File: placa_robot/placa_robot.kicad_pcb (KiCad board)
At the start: 2 copper layers, 75 x 80 mm, 26 parts, among them IC1 MSP430FR2355TPT, J1 Conn_01x03, J2 Conn_01x01, J3 Conn_02x04_Odd_Even, J4 conn_DFrobot, SW1 SW_Push, U1 LM324, Y1 Crystal

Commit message: Desacoplos y limitador
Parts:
- added C6: 100n, Capacitor_SMD:C_0805_2012Metric_Pad1.18x1.45mm_HandSolder, F.Cu at (86.0, 70.5)
- added TP1: TestPoint, Connector_PinHeader_2.54mm:PinHeader_1x01_P2.54mm_Vertical, F.Cu at (78.5, 53.7)
- added TP10: TestPoint, Connector_PinHeader_2.54mm:PinHeader_1x01_P2.54mm_Vertical, F.Cu at (83.2, 53.7)
- added TP11: TestPoint, Connector_PinHeader_2.54mm:PinHeader_1x01_P2.54mm_Vertical, F.Cu at (83.2, 58.4)
- added TP12: TestPoint, Connector_PinHeader_2.54mm:PinHeader_1x01_P2.54mm_Vertical, F.Cu at (83.2, 63.0)
- added TP13: TestPoint, Connector_PinHeader_2.54mm:PinHeader_1x01_P2.54mm_Vertical, F.Cu at (87.8, 53.7)
- added TP14: TestPoint, Connector_PinHeader_2.54mm:PinHeader_1x01_P2.54mm_Vertical, F.Cu at (87.8, 58.4)
- added TP15: TestPoint, Connector_PinHeader_2.54mm:PinHeader_1x01_P2.54mm_Vertical, F.Cu at (87.8, 63.0)
- added TP16: TestPoint, Connector_PinHeader_2.54mm:PinHeader_1x01_P2.54mm_Vertical, F.Cu at (92.5, 53.7)
- added TP17: TestPoint, Connector_PinHeader_2.54mm:PinHeader_1x01_P2.54mm_Vertical, F.Cu at (92.5, 58.4)
- added TP18: TestPoint, Connector_PinHeader_2.54mm:PinHeader_1x01_P2.54mm_Vertical, F.Cu at (92.5, 63.0)
- added TP2: TestPoint, Connector_PinHeader_2.54mm:PinHeader_1x01_P2.54mm_Vertical, F.Cu at (78.5, 58.4)
- added TP6: TestPoint, Connector_PinHeader_2.54mm:PinHeader_1x01_P2.54mm_Vertical, F.Cu at (78.5, 63.0)
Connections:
- net Net-(IC1-P2.6/MCLK/XOUT) renamed /XOUT
- net Net-(IC1-P2.7/TB0CLK/XIN) renamed /XIN
- IC1 pad 6: unconnected-(IC1-DVCC-Pad6) -> +3.3V
- IC1 pad 7: unconnected-(IC1-DVSS-Pad7) -> GND
- JP1 pad 1: +3.3V -> /Pantalla_LCD
- LCD1 pad 6: +3.3V -> /Pantalla_LCD
- LCD1 pad 7: GND -> Net-(LCD1-K)
- RV1 pad 1: unconnected-(RV1-Pad1) -> /Photo2
- RV1 pad 2: /Photo2 -> GND
- RV2 pad 1: unconnected-(RV2-Pad1) -> /Photo1
- RV2 pad 2: /Photo1 -> GND
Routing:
- net /XOUT: track 0.00 -> 3.86 mm
- net /XIN: track 0.00 -> 3.28 mm
- net GND: track 1.50 -> 4.03 mm, vias 1 -> 2

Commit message: Errores layout
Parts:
- removed TP1, TP10, TP11, TP12, TP13, TP14, TP15, TP16, TP17, TP18, TP2, TP6: TestPoint, Connector_PinHeader_2.54mm:PinHeader_1x01_P2.54mm_Vertical
- added C7: 100n, Capacitor_SMD:C_0805_2012Metric_Pad1.18x1.45mm_HandSolder, F.Cu at (141.5, 111.2)
- added R1: 1k, Resistor_SMD:R_0805_2012Metric_Pad1.20x1.40mm_HandSolder, F.Cu at (165.2, 67.2)
- R10, R9: footprint Connector_PinHeader_2.54mm:PinHeader_1x02_P2.54mm_Horizontal -> Connector_PinHeader_2.54mm:PinHeader_1x02_P2.54mm_Vertical
- moved C6 67.4 mm to (153.2, 73.8), turned to 180 degrees
- moved C4 15.1 mm to (149.0, 65.6), turned to 180 degrees
- moved C2 13.4 mm to (149.2, 71.2), turned to 180 degrees
- moved R10 2.75 mm to (179.0, 117.2)
- moved S2 2.28 mm to (141.6, 100.6)
- moved R9 2.24 mm to (114.5, 118.0)
- moved JP1 2.00 mm to (179.0, 66.2)
- moved Y1 0.99 mm to (148.0, 69.3)
- moved J2 0.75 mm to (168.2, 118.0)
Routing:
- net GND: track 4.03 -> 21.9 mm, vias 2 -> 10
- net +3.3V: track 11.0 -> 27.1 mm
- net /Pantalla_LCD: track 0.00 -> 7.64 mm
- net /Photo1: track 77.9 -> 82.3 mm
- net Net-(LCD1-K): track 0.00 -> 3.28 mm
- net /XOUT: track 3.86 -> 6.95 mm
- net /XIN: track 3.28 -> 6.04 mm
- net Net-(S2-2'): track 16.4 -> 19.0 mm
- net /JOY_BOTTON: track 63.5 -> 65.9 mm
- net /P2: track 13.4 -> 11.7 mm
- net Net-(U1C--): track 36.0 -> 37.6 mm
- net /Photo2: track 61.8 -> 63.2 mm
- net /P1: track 15.7 -> 14.3 mm
- net /P0: track 17.3 -> 16.0 mm
- net /LEFT: track 9.80 -> 10.4 mm
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
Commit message: Placa acabada
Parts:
- removed C3: 100n, Capacitor_SMD:C_0805_2012Metric_Pad1.18x1.45mm_HandSolder
- moved R13 3.60 mm to (175.4, 58.5)
- moved R14 3.60 mm to (175.4, 54.5)
- moved C6 0.21 mm to (153.5, 73.8)
- moved C4 0.14 mm to (149.1, 65.6)
- moved Y1 0.07 mm to (148.1, 69.3)
- moved C2 0.06 mm to (149.1, 71.2)
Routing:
- net +3.3V: track 27.1 -> 32.2 mm, vias 0 -> 6
- net /MCU_RST: track 81.0 -> 85.7 mm
- net GND: track 21.9 -> 26.3 mm
- net /SDA: track 79.9 -> 76.3 mm
- net /SCL: track 80.3 -> 77.4 mm
- net /WIFI_RXD: track 60.2 -> 61.1 mm

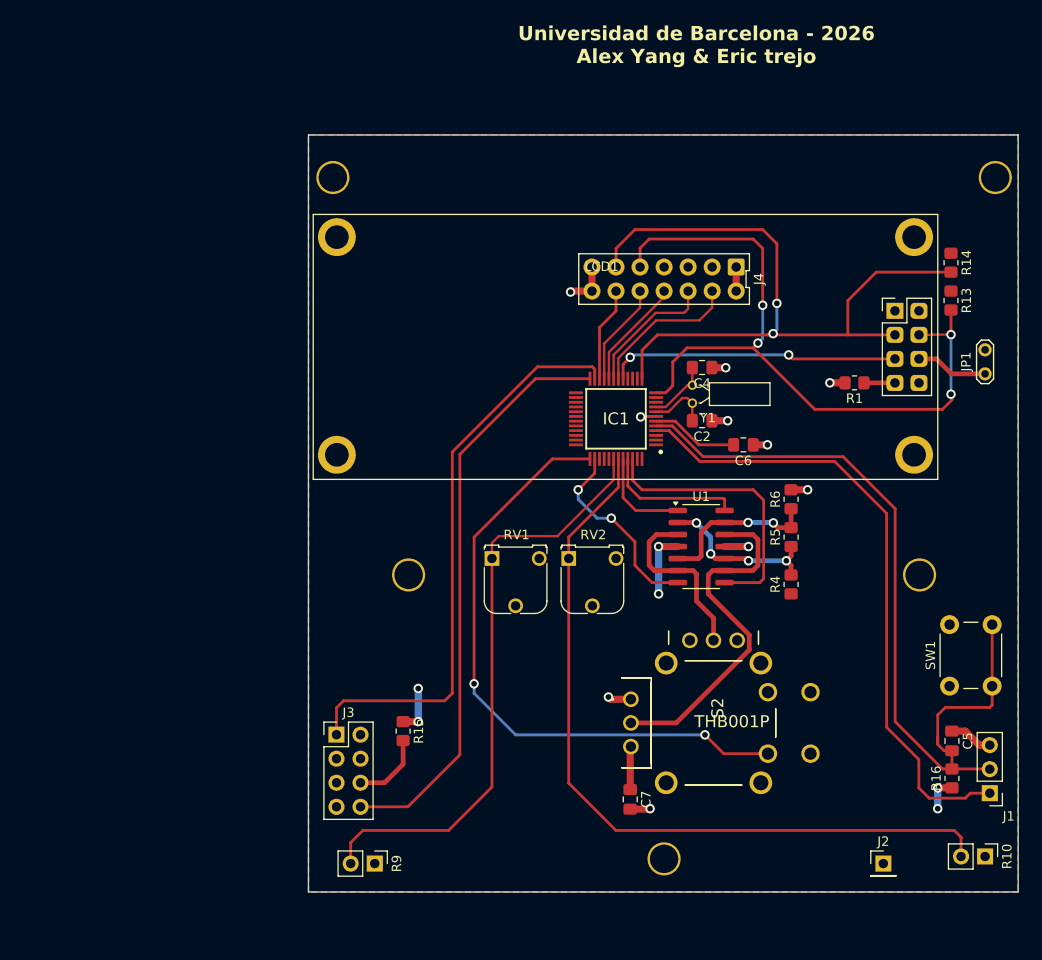
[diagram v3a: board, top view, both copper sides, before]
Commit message: Serigrafia y testpoints colocados
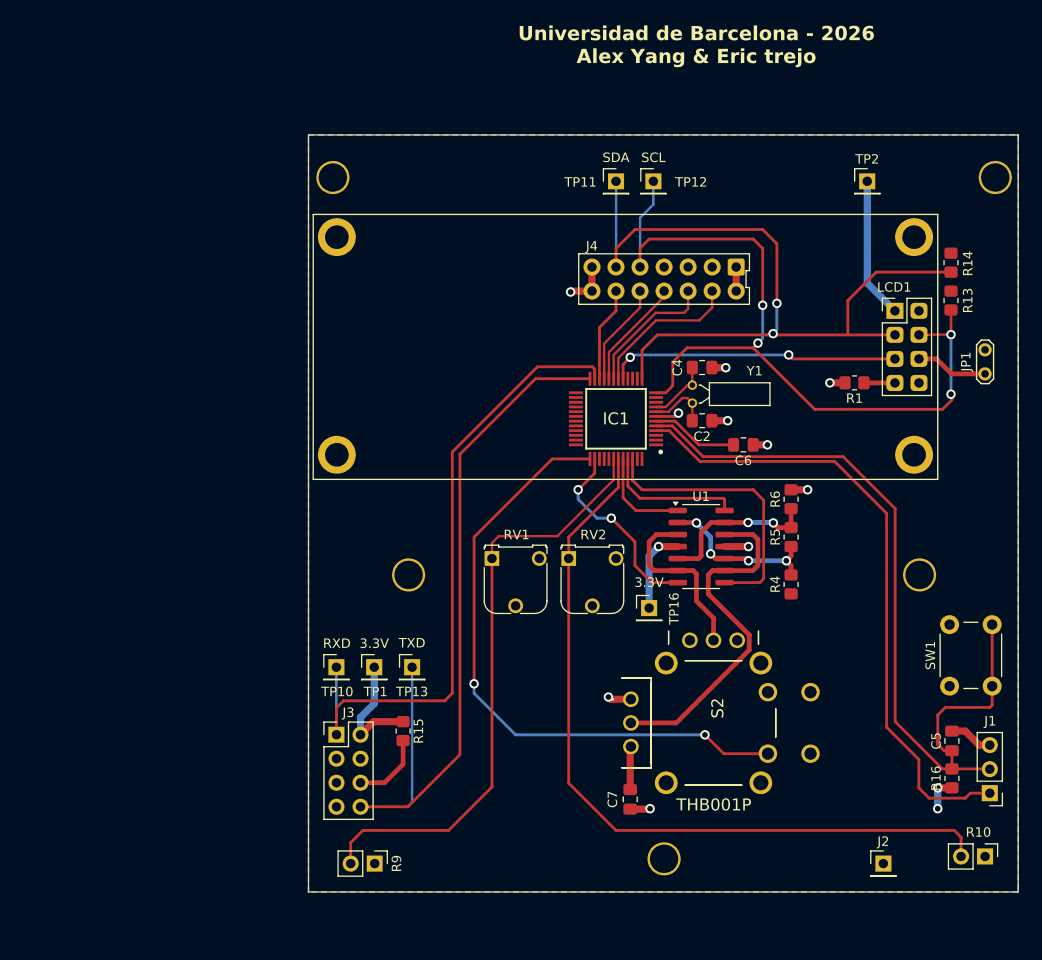
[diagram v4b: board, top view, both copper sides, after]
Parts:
- added SCL: TestPoint, Connector_PinHeader_2.54mm:PinHeader_1x01_P2.54mm_Vertical, F.Cu at (143.9, 45.9)
- added SDA: TestPoint, Connector_PinHeader_2.54mm:PinHeader_1x01_P2.54mm_Vertical, F.Cu at (140.0, 45.9)
- added TP1: TestPoint, Connector_PinHeader_2.54mm:PinHeader_1x01_P2.54mm_Vertical, F.Cu at (114.5, 97.2)
- added TP10: TestPoint, Connector_PinHeader_2.54mm:PinHeader_1x01_P2.54mm_Vertical, F.Cu at (110.5, 97.2)
- added TP13: TestPoint, Connector_PinHeader_2.54mm:PinHeader_1x01_P2.54mm_Vertical, F.Cu at (118.5, 97.2)
- added TP16: TestPoint, Connector_PinHeader_2.54mm:PinHeader_1x01_P2.54mm_Vertical, F.Cu at (143.5, 91.0)
- added TP2: TestPoint, Connector_PinHeader_2.54mm:PinHeader_1x01_P2.54mm_Vertical, F.Cu at (166.6, 45.9)
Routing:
- net +3.3V: track 32.2 -> 56.7 mm, vias 6 -> 3
- net /WIFI_TXD: track 61.6 -> 81.5 mm
- net /SCL: track 77.4 -> 87.1 mm
- net /SDA: track 76.3 -> 85.3 mm
- net /WIFI_RXD: track 61.1 -> 68.2 mm
- net GND: track 26.3 -> 27.1 mm
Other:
- board text added: "3.3V"
- board text added: "C4"
- board text added: "RXD"
- board text added: "TP11"
- board text added: "TP12"
- board text added: "TXD"

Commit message: Arreglos varios
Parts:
- removed TP2: TestPoint, Connector_PinHeader_2.54mm:PinHeader_1x01_P2.54mm_Vertical
- moved C5 36.2 mm to (156.2, 74.5), turned to 180 degrees
- moved R16 20.9 mm to (180.3, 88.7), turned to -90 degrees
- moved R14 11.5 mm to (166.0, 61.1)
- moved SDA 8.28 mm to (131.7, 45.9)
- moved SDL 8.28 mm to (135.7, 45.9)
- moved C6 4.43 mm to (149.1, 74.4)
- moved R13 2.63 mm to (175.6, 61.1)
- renumbered SCL to SDL
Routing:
- net +3.3V: track 56.7 -> 32.0 mm, vias 3 -> 1
- net /SDA: track 85.3 -> 66.2 mm
- net /MCU_RST: track 85.7 -> 76.8 mm
- net GND: track 27.1 -> 22.5 mm, vias 10 -> 11
- net /LCD_RST: track 30.8 -> 33.8 mm, vias 2 -> 1
- net /SCL: track 87.1 -> 84.4 mm, vias 4 -> 1
- net /SBW: track 66.6 -> 65.6 mm
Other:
- board text removed: "TP11"
- board text removed: "TP12"
